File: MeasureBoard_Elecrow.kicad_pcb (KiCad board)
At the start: 2 copper layers, 60 x 91 mm, 133 parts, among them J1 Conn_01x04, J1 Conn_02x05_Odd_Even, J10 TEST_1P, J11 TEST_1P, J12 TEST_1P, J13 BARREL_JACK, J14 CONN_01X02, J15 Conn_02x05_Odd_Even, J16 Conn_01x06, J17 GS3, J18 USB_OTG, J19 Conn_01x02, J2 Conn_01x06, J20 Conn_01x02, J21 Conn_01x03, J22 Conn_01x03, J23 Conn_01x03, J24 Conn_01x03, J25 Conn_01x03, J26 Conn_01x03, J27 Conn_02x05_Odd_Even, J3 Conn_01x04, J4 GS3, J5 GS2, J6 Conn_01x04, J7 Conn_01x03, J8 Conn_01x04, J9 TEST_1P, SW1 DIP_SW_2P, SW2 SKRPACE010, SW3 SKRPACE010, SW4 SKRPACE010, U1 L7805, U2 AP1117-33, U3 STM32F103CBTx, U4 NC7SZ08, U5 SP3481CN, U6 NC7WZ241, U7 MCP2562-E-SN, U8 AM26LV32, Y1 Crystal

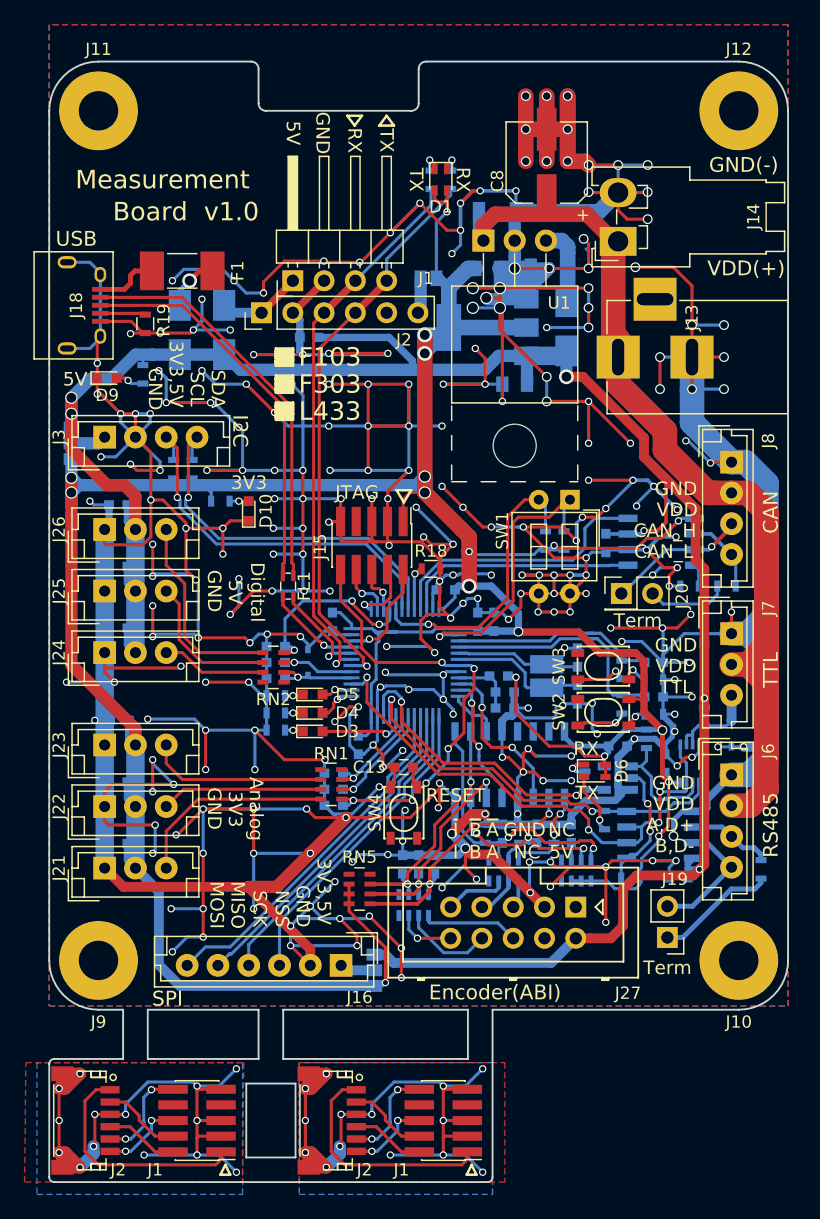
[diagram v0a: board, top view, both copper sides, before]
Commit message: USB，D+周りの変更をAWにまで適用した．
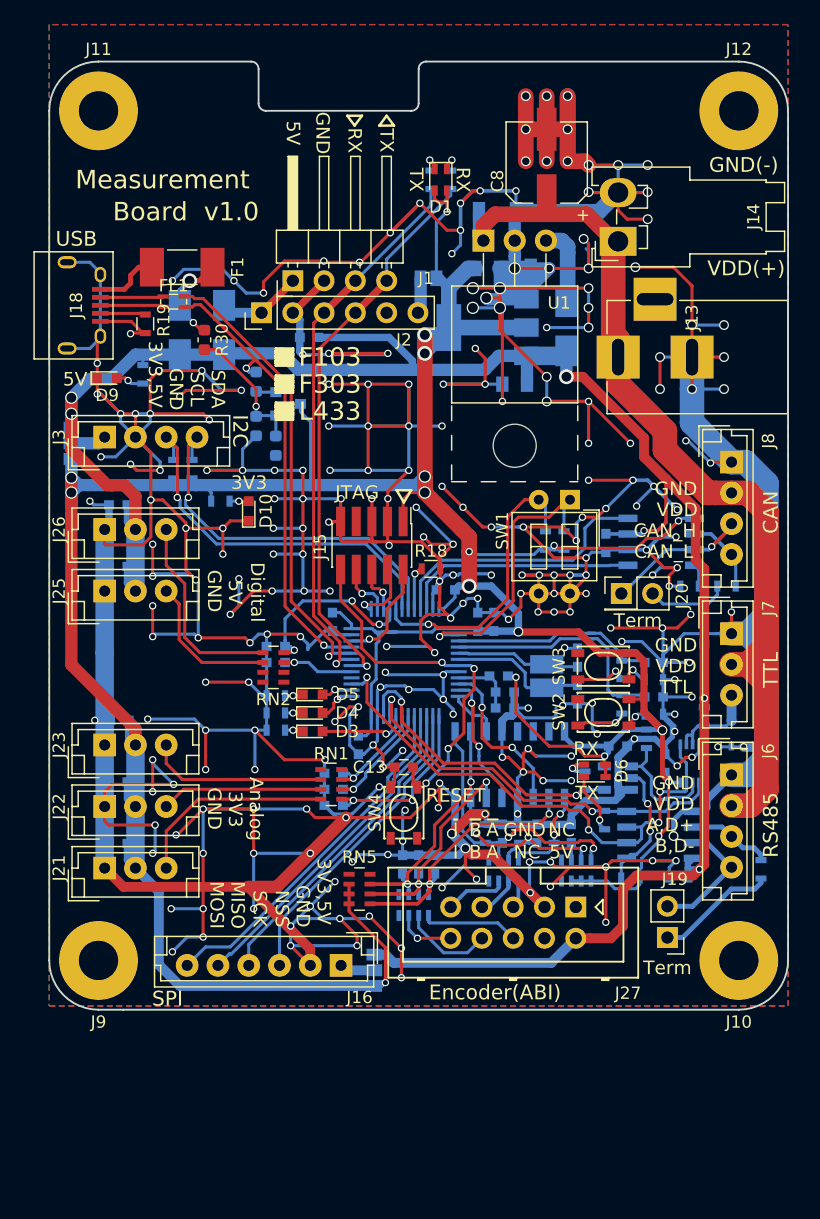
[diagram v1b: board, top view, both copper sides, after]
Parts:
- removed C29: 220p, Capacitors_SMD:C_0603
- removed C32: 0.1u, Capacitors_SMD:C_0603
- removed D7: D_Zener_Small, Diodes_SMD:D_SOD-323
- removed the J1 at (142.0, 141.0)
- removed the J1 at (122.0, 141.0)
- removed the J2 at (133.0, 141.0)
- removed the J2 at (113.0, 141.0)
- removed J24: Conn_01x03, Connectors_JST:JST_EH_B03B-EH-A_03x2.50mm_Straight
- added Q1: BSS138, Package_TO_SOT_SMD:SOT-23, B.Cu at (129.4, 82.8)
- added R29: 1.5k, Resistor_SMD:R_0603_1608Metric, B.Cu at (126.8, 81.0)
- added R30: 10k, Resistor_SMD:R_0603_1608Metric, F.Cu at (122.6, 77.6)
- added R31: 36k, Resistor_SMD:R_0603_1608Metric, B.Cu at (126.8, 84.6)
- added R32: R, Resistor_SMD:R_0603_1608Metric, B.Cu at (128.4, 86.2)
- moved FL1 24.9 mm to (120.1, 74.5), turned to 0 degrees
- moved F1 0.30 mm to (120.8, 71.7)
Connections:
- net Net-(FL1-Pad1) renamed /USB/USB_-
- net Net-(FL1-Pad3) renamed /USB/USB_+
- J10 pad 1: Net-(J10-Pad1) -> (no net)
- J11 pad 1: Net-(J11-Pad1) -> (no net)
- J12 pad 1: Net-(J12-Pad1) -> (no net)
- J13 pad 3: Net-(J13-Pad3) -> (no net)
- J15 pad 7: Net-(J15-Pad7) -> (no net)
- J2 pad 5: Net-(J2-Pad5) -> (no net)
- J27 pad 1: Net-(J27-Pad1) -> (no net)
- J27 pad 4: Net-(J27-Pad4) -> (no net)
- J9 pad 1: Net-(J9-Pad1) -> (no net)
- R1 pad 2: Net-(D1-Pad2) -> Net-(D1-Pad4)
- R2 pad 2: Net-(D1-Pad4) -> Net-(D1-Pad2)
- RN1 pad 4: Net-(RN1-Pad4) -> (no net)
- RN1 pad 5: Net-(RN1-Pad5) -> (no net)
- RN2 pad 1: Net-(RN2-Pad1) -> (no net)
- RN2 pad 2: /IN_Di/DI3_LPF -> (no net)
- RN2 pad 7: Net-(J24-Pad3) -> (no net)
- RN2 pad 8: Net-(RN2-Pad8) -> (no net)
- RN3 pad 4: Net-(RN3-Pad4) -> (no net)
- RN3 pad 5: Net-(RN3-Pad5) -> (no net)
- RN4 pad 4: Net-(RN4-Pad4) -> (no net)
- RN4 pad 5: Net-(RN4-Pad5) -> (no net)
- RN5 pad 4: Net-(RN5-Pad4) -> (no net)
- RN5 pad 5: Net-(RN5-Pad5) -> (no net)
- RN6 pad 1: Net-(RN6-Pad1) -> (no net)
- RN6 pad 8: Net-(RN6-Pad8) -> (no net)
- SW2 pad 1: Net-(SW2-Pad1) -> (no net)
- SW3 pad 1: Net-(SW3-Pad1) -> (no net)
- SW4 pad 1: Net-(SW4-Pad1) -> (no net)
- SW4 pad 3: Net-(SW4-Pad3) -> (no net)
- U3 pad 28: /IN_Di/DI3_LPF -> /USB_EN
- U8 pad 13: Net-(U8-Pad13) -> (no net)
- U8 pad 14: Net-(U8-Pad14) -> (no net)
- U8 pad 15: Net-(U8-Pad15) -> (no net)
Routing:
- net GND: track 1267.9 -> 1125.2 mm, vias 295 -> 256
- net Vtag: track 37.6 -> 0.00 mm
- net /USB/D+: track 7.68 -> 37.6 mm, vias 1 -> 2
- net /USB/D-: track 8.24 -> 37.1 mm
- net /USB/USB_-: track 33.3 -> 5.13 mm
- net /USB/USB_+: track 32.6 -> 5.15 mm
- net nRST: track 16.9 -> 0.00 mm, vias 4 -> 0
- net SWO: track 13.3 -> 0.00 mm, vias 4 -> 0
- net SWCLK: track 13.0 -> 0.00 mm
- net SWDIO: track 11.9 -> 0.00 mm
- net Net-(Q1-Pad1): track 0.00 -> 11.1 mm, vias 0 -> 1
- net Net-(J24-Pad3): track 9.08 -> 0.00 mm
- net +5V: track 183.9 -> 176.6 mm
- net /IN_Di/DI3_LPF: track 6.97 -> 0.00 mm, vias 1 -> 0
- net +3V3: track 299.2 -> 306.2 mm
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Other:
- board size 60 x 91 mm -> 60 x 77 mm
- board text removed: "SWD-JTAG10 adaptor"
